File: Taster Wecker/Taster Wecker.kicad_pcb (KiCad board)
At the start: 2 copper layers, 20 parts, among them J1 Conn_01x09_Male

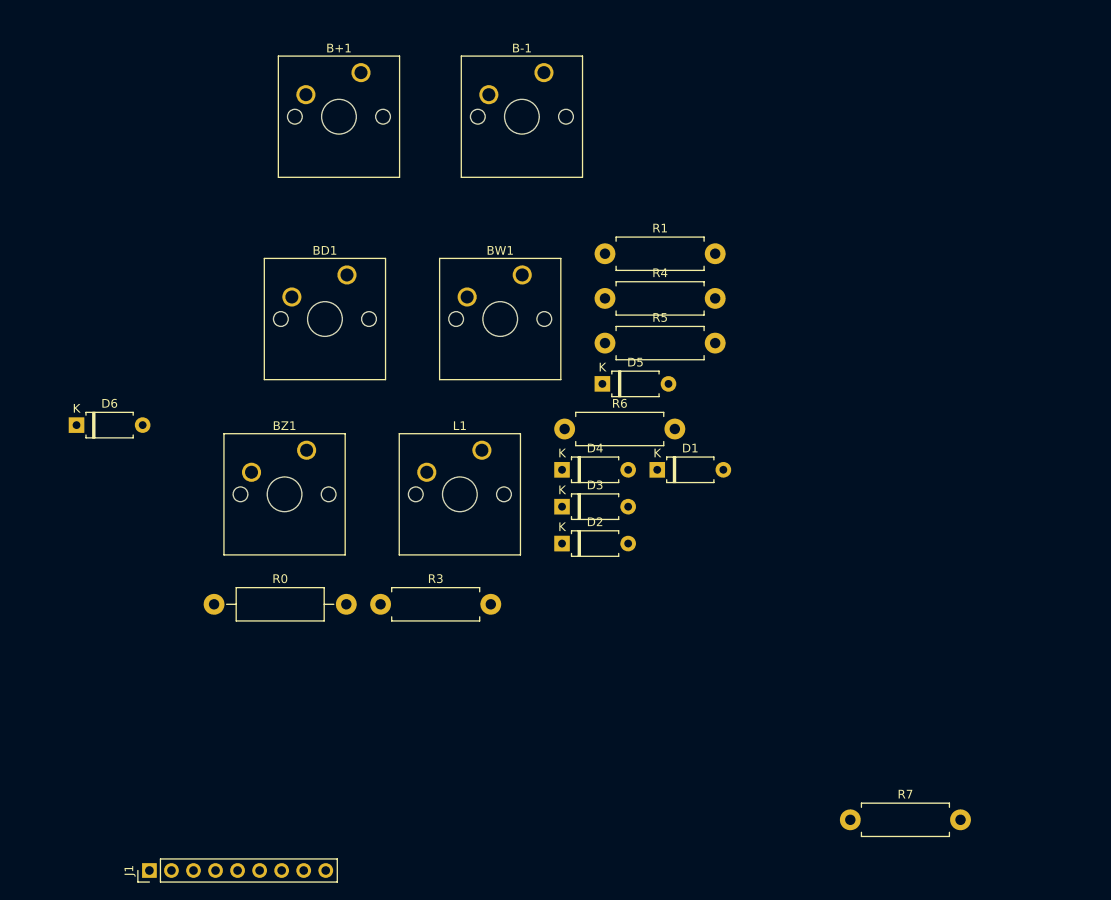
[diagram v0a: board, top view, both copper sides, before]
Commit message: LEDs ginzugefügt, die an gehen, wenn man einen Knopf drückt.
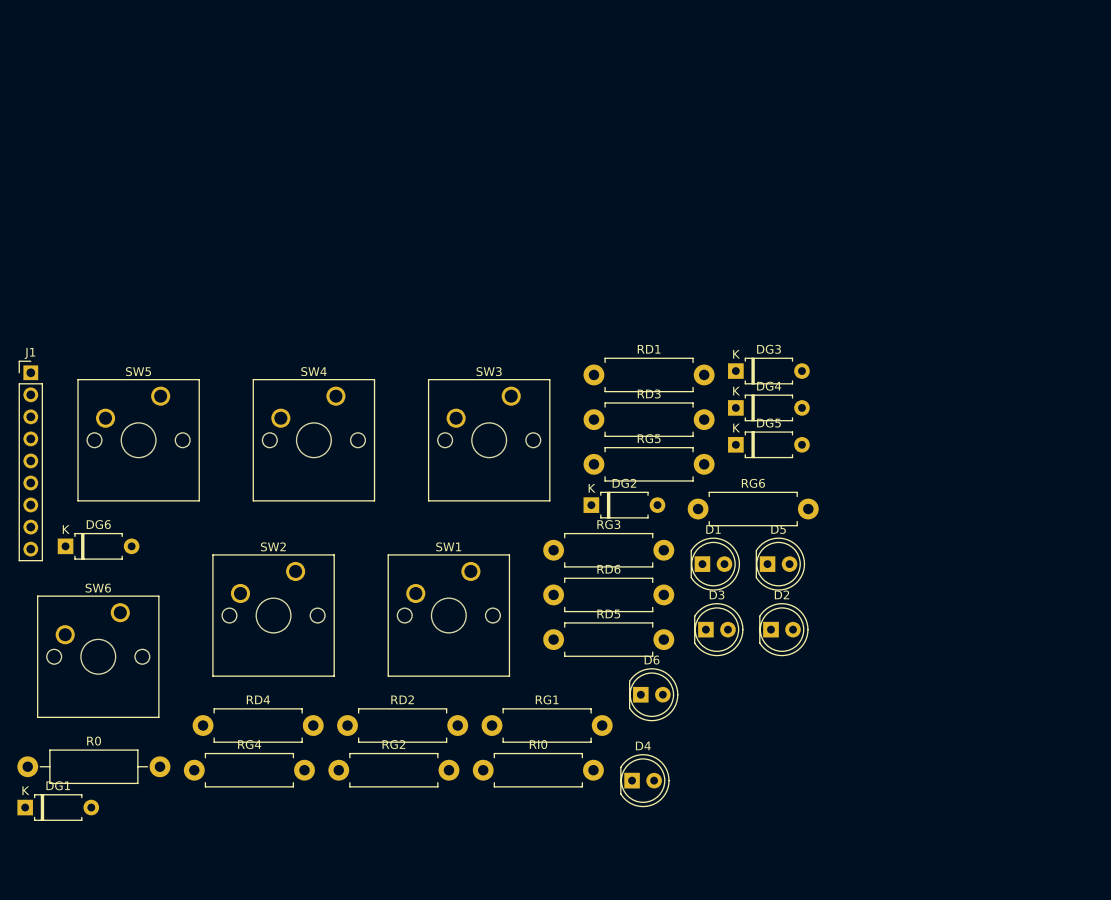
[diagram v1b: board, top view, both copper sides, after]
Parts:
- removed B+1, B-1, BD1, BW1, BZ1, L1: SW_Push, Button_Switch_Keyboard:SW_Cherry_MX_1.00u_PCB
- removed R1, R3, R4, R5, R6, R7: 10k, Resistor_THT:R_Axial_DIN0411_L9.9mm_D3.6mm_P12.70mm_Horizontal
- added DG1: DIODE, Diode_THT:D_A-405_P7.62mm_Horizontal, F.Cu at (89.1, 110.6)
- added DG2: DIODE, Diode_THT:D_A-405_P7.62mm_Horizontal, F.Cu at (154.3, 75.7)
- added DG3: DIODE, Diode_THT:D_A-405_P7.62mm_Horizontal, F.Cu at (171.0, 60.3)
- added DG4: DIODE, Diode_THT:D_A-405_P7.62mm_Horizontal, F.Cu at (171.0, 64.5)
- added DG5: DIODE, Diode_THT:D_A-405_P7.62mm_Horizontal, F.Cu at (171.0, 68.8)
- added DG6: DIODE, Diode_THT:D_A-405_P7.62mm_Horizontal, F.Cu at (93.7, 80.5)
- added RD1: 100, Resistor_THT:R_Axial_DIN0411_L9.9mm_D3.6mm_P12.70mm_Horizontal, F.Cu at (154.6, 60.7)
- added RD2: 100, Resistor_THT:R_Axial_DIN0411_L9.9mm_D3.6mm_P12.70mm_Horizontal, F.Cu at (126.2, 101.1)
- added RD3: 100, Resistor_THT:R_Axial_DIN0411_L9.9mm_D3.6mm_P12.70mm_Horizontal, F.Cu at (154.6, 65.9)
- added RD4: 100, Resistor_THT:R_Axial_DIN0411_L9.9mm_D3.6mm_P12.70mm_Horizontal, F.Cu at (109.6, 101.1)
- added RD5: 100, Resistor_THT:R_Axial_DIN0411_L9.9mm_D3.6mm_P12.70mm_Horizontal, F.Cu at (150.0, 91.2)
- added RD6: 100, Resistor_THT:R_Axial_DIN0411_L9.9mm_D3.6mm_P12.70mm_Horizontal, F.Cu at (150.0, 86.1)
- added RG1: 10k, Resistor_THT:R_Axial_DIN0411_L9.9mm_D3.6mm_P12.70mm_Horizontal, F.Cu at (142.9, 101.1)
- added RG2: 10k, Resistor_THT:R_Axial_DIN0411_L9.9mm_D3.6mm_P12.70mm_Horizontal, F.Cu at (125.2, 106.3)
- added RG3: 10k, Resistor_THT:R_Axial_DIN0411_L9.9mm_D3.6mm_P12.70mm_Horizontal, F.Cu at (150.0, 80.9)
- added RG4: 10k, Resistor_THT:R_Axial_DIN0411_L9.9mm_D3.6mm_P12.70mm_Horizontal, F.Cu at (108.5, 106.3)
- added RG5: 10k, Resistor_THT:R_Axial_DIN0411_L9.9mm_D3.6mm_P12.70mm_Horizontal, F.Cu at (154.6, 71.0)
- added RG6: 10k, Resistor_THT:R_Axial_DIN0411_L9.9mm_D3.6mm_P12.70mm_Horizontal, F.Cu at (166.6, 76.2)
- added RI0: 100, Resistor_THT:R_Axial_DIN0411_L9.9mm_D3.6mm_P12.70mm_Horizontal, F.Cu at (141.8, 106.3)
- added SW1: SW_L, Button_Switch_Keyboard:SW_Cherry_MX_1.00u_PCB, F.Cu at (140.4, 83.4)
- added SW2: SW_D, Button_Switch_Keyboard:SW_Cherry_MX_1.00u_PCB, F.Cu at (120.2, 83.4)
- added SW3: SW_W, Button_Switch_Keyboard:SW_Cherry_MX_1.00u_PCB, F.Cu at (145.1, 63.2)
- added SW4: SW_Z, Button_Switch_Keyboard:SW_Cherry_MX_1.00u_PCB, F.Cu at (124.9, 63.2)
- added SW5: SW_-, Button_Switch_Keyboard:SW_Cherry_MX_1.00u_PCB, F.Cu at (104.7, 63.2)
- added SW6: SW_+, Button_Switch_Keyboard:SW_Cherry_MX_1.00u_PCB, F.Cu at (100.0, 88.1)
- D1, D2, D3, D4, D5, D6: value DIODE -> LED; footprint Diode_THT:D_A-405_P7.62mm_Horizontal -> LED_THT:LED_D5.0mm
- moved D6 72.1 mm to (160.0, 97.6)
- moved J1 59.0 mm to (89.7, 60.5), turned to 0 degrees
- moved D4 36.7 mm to (159.0, 107.5)
- moved R0 28.5 mm to (89.4, 105.9)
- moved D5 28.2 mm to (174.6, 82.5)
- moved D2 26.0 mm to (175.0, 90.1)
- moved D3 21.8 mm to (167.5, 90.1)
- moved D1 12.1 mm to (167.1, 82.5)
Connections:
- D2 pad 2: Net-(D1-Pad2) -> Net-(D2-Pad2)
- D3 pad 2: Net-(D1-Pad2) -> Net-(D3-Pad2)
- D4 pad 2: Net-(D1-Pad2) -> Net-(D4-Pad2)
- D5 pad 2: Net-(D1-Pad2) -> Net-(D5-Pad2)
- D6 pad 2: Net-(D1-Pad2) -> Net-(D6-Pad2)
- J1 pad 3: Net-(D1-Pad2) -> Net-(J1-Pad3)

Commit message: PCB Layout für Die Taster erstellt
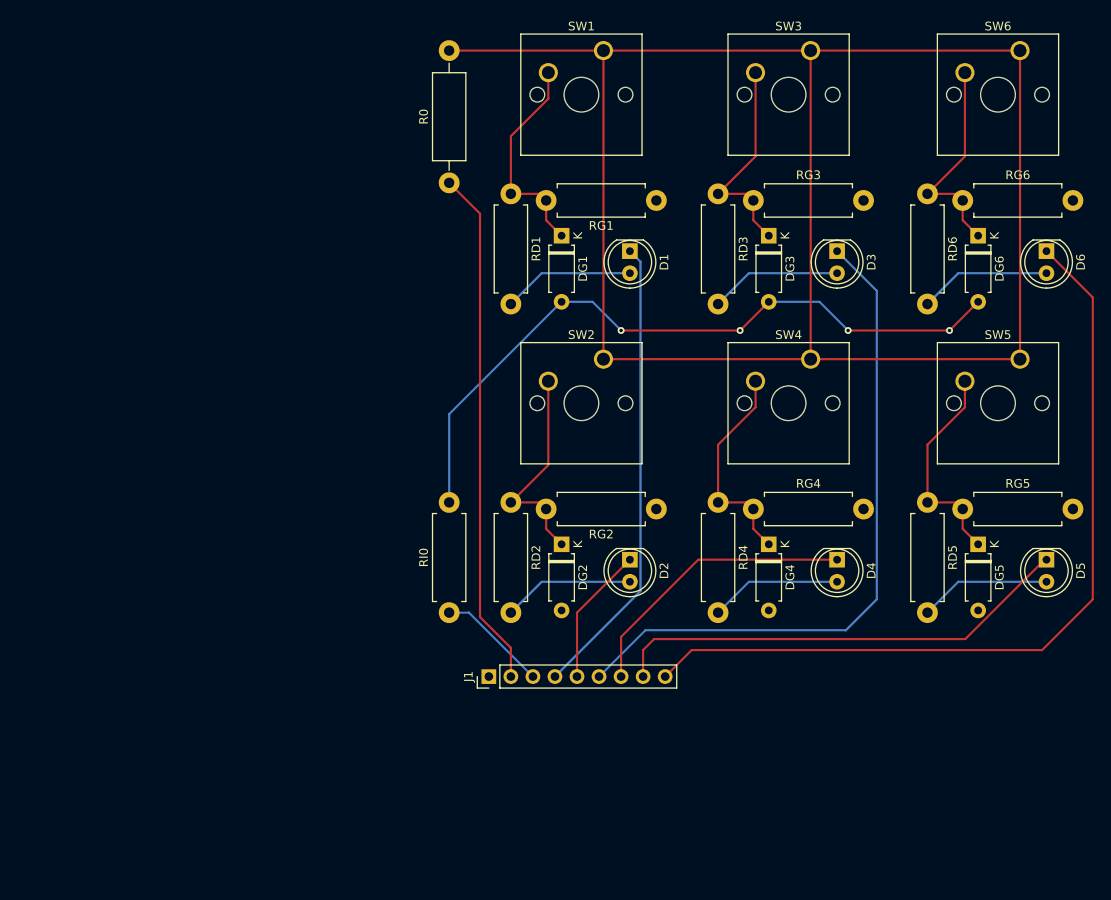
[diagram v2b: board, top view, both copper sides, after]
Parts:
- moved SW6 122.3 mm to (203.7, 23.4)
- moved DG6 111.1 mm to (198.9, 44.7), turned to 270 degrees
- moved SW5 99.1 mm to (203.7, 58.9)
- moved DG1 90.4 mm to (150.9, 44.7), turned to 270 degrees
- moved R0 83.0 mm to (137.9, 38.6), turned to 90 degrees
- moved RG4 71.1 mm to (173.0, 76.2)
- moved D6 69.3 mm to (206.8, 46.5), turned to 270 degrees
- moved RD4 64.7 mm to (168.9, 75.4), turned to 270 degrees
- moved RG1 63.4 mm to (161.8, 40.6), turned to 180 degrees
- moved J1 63.3 mm to (142.5, 95.5), turned to 90 degrees
- moved RD6 63.2 mm to (193.0, 39.9), turned to 270 degrees
- moved SW1 61.9 mm to (155.7, 23.4)
- moved SW4 54.9 mm to (179.6, 58.9)
- moved SW3 52.7 mm to (179.6, 23.4)
- moved RG2 47.4 mm to (161.8, 76.2), turned to 180 degrees
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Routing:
- net Net-(R0-Pad2): track 0.00 -> 220.5 mm
- net Net-(D6-Pad1): track 0.00 -> 95.3 mm
- net Net-(DG1-Pad2): track 0.00 -> 82.0 mm, vias 0 -> 4
- net Net-(D3-Pad1): track 0.00 -> 77.7 mm
- net +5V: track 0.00 -> 59.8 mm
- net Net-(D5-Pad1): track 0.00 -> 53.8 mm
- net Net-(D1-Pad1): track 0.00 -> 53.6 mm
- net Net-(D4-Pad1): track 0.00 -> 33.1 mm
- net Net-(DG6-Pad1): track 0.00 -> 24.9 mm
- net Net-(DG1-Pad1): track 0.00 -> 24.9 mm
- net Net-(DG5-Pad1): track 0.00 -> 24.9 mm
- net Net-(DG2-Pad1): track 0.00 -> 24.9 mm
- net Net-(DG3-Pad1): track 0.00 -> 24.9 mm
- net Net-(DG4-Pad1): track 0.00 -> 24.9 mm
- net Net-(D2-Pad1): track 0.00 -> 16.0 mm
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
